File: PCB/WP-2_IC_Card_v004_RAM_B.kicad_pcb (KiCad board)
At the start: 2 copper layers, 45 x 54 mm, 11 parts, among them J1 Conn_01x38_Female, U1 SRAM 128Kx8 5v Parallel, U2 SRAM 128Kx8 5v Parallel

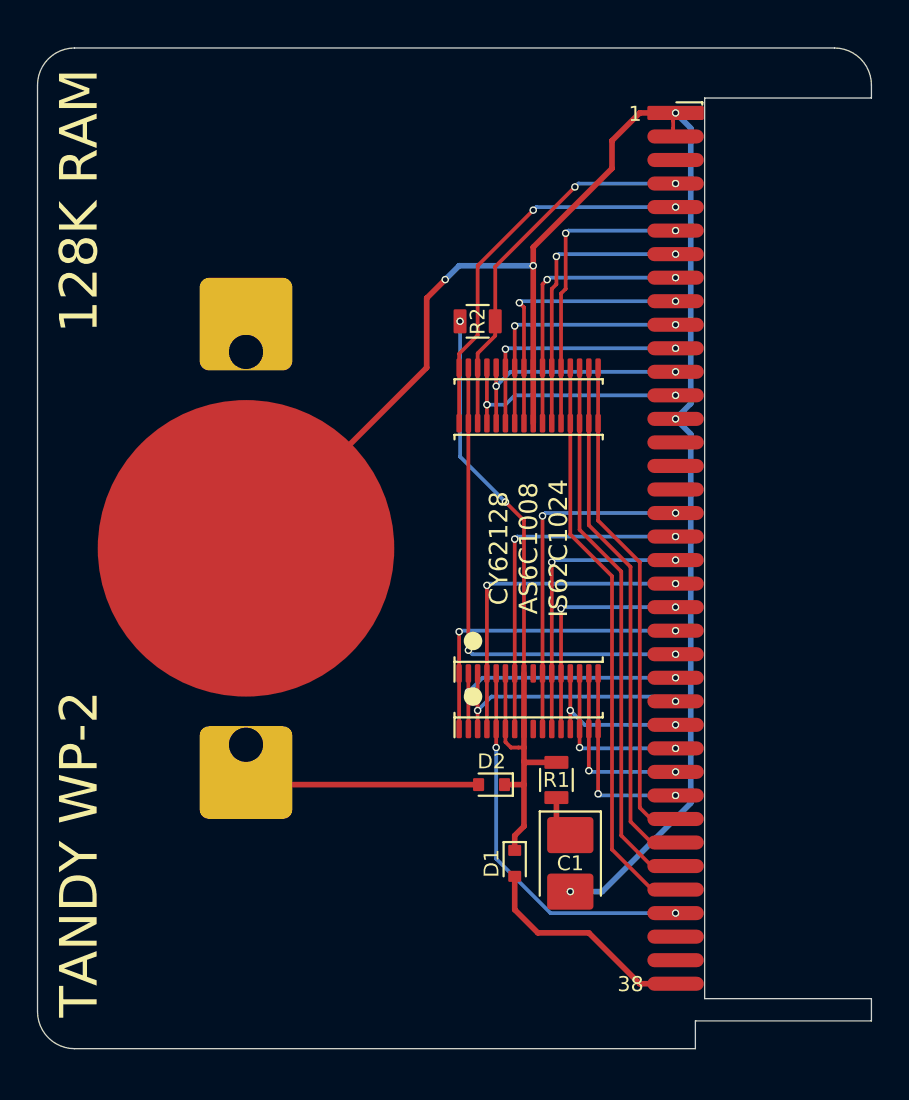
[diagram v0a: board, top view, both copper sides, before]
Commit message: reroute battery traces. cosmetics
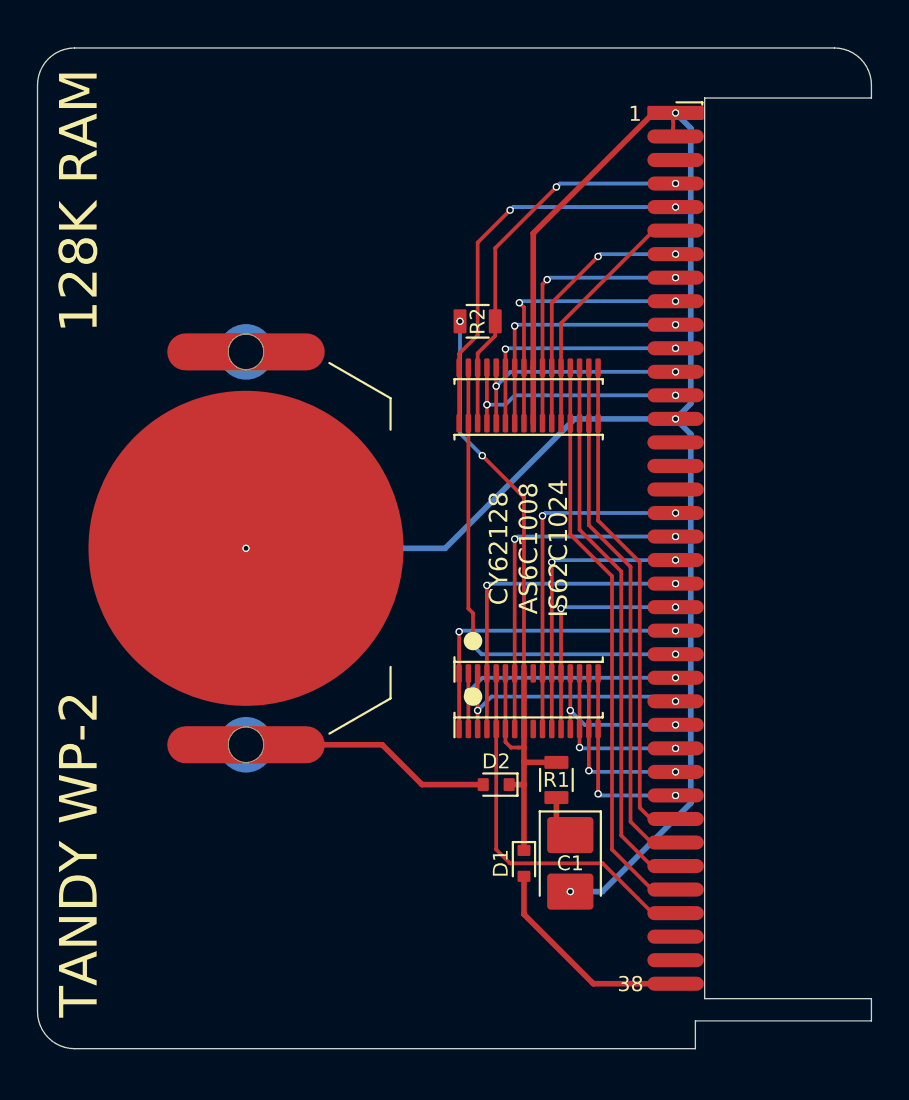
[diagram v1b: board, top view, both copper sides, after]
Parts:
- moved D1 0.50 mm to (149.0, 116.7)
- moved D2 0.25 mm to (147.5, 112.4)
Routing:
- net /D0: track 16.3 -> 13.6 mm, vias 2 -> 0
- net GND: track 92.3 -> 93.9 mm, vias 5 -> 4
- net /D1: track 15.6 -> 14.3 mm
- net /~OE: track 20.9 -> 21.6 mm
- net /~CE1: track 20.4 -> 21.0 mm
- net /R~W: track 20.9 -> 20.6 mm, vias 2 -> 0

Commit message: CR2016 battery holder
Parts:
- BT1: value Battery 2016 3v -> Battery CR2016 3v
- D1, D2: value D_Schottky_Small_ALT -> 1SS389
- R1: value 470 -> 4.7K
